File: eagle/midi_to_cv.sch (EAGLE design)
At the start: 46 parts, among them IC2 4504N, IC3 4099N, U1 ATMEGA328P_PDIP

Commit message: a manual start
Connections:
- net N$13: now also U1.PC2(ADC2); no longer U1.PC0(ADC0)
- net N$25: now also U1.PC0(ADC0); no longer U1.PC2(ADC2)
- net N$37: now also IC3A.!E; no longer IC3A.D
- net N$38: now also IC3A.D; no longer IC3A.!E
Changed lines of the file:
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@@
 <pinref part="IC2" gate="A" pin="DO"/>
 <wire x1="86.36" y1="66.04" x2="91.44" y2="66.04" width="0.1524" layer="91"/>
-<wire x1="91.44" y1="66.04" x2="91.44" y2="30.48" width="0.1524" layer="91"/>
-<pinref part="IC3" gate="A" pin="D"/>
-<wire x1="91.44" y1="30.48" x2="99.06" y2="30.48" width="0.1524" layer="91"/>
+<wire x1="91.44" y1="66.04" x2="91.44" y2="33.02" width="0.1524" layer="91"/>
+<pinref part="IC3" gate="A" pin="!E"/>
+<wire x1="99.06" y1="33.02" x2="91.44" y2="33.02" width="0.1524" layer="91"/>
 </segment>
 </net>
@@
 <pinref part="IC2" gate="A" pin="EO"/>
 <wire x1="86.36" y1="63.5" x2="88.9" y2="63.5" width="0.1524" layer="91"/>
-<wire x1="88.9" y1="63.5" x2="88.9" y2="33.02" width="0.1524" layer="91"/>
-<pinref part="IC3" gate="A" pin="!E"/>
-<wire x1="99.06" y1="33.02" x2="88.9" y2="33.02" width="0.1524" layer="91"/>
+<wire x1="88.9" y1="63.5" x2="88.9" y2="30.48" width="0.1524" layer="91"/>
+<pinref part="IC3" gate="A" pin="D"/>
+<wire x1="88.9" y1="30.48" x2="99.06" y2="30.48" width="0.1524" layer="91"/>
 </segment>
 </net>
@@
 </segment>
 </net>
-<net name="N$13" class="0">
-<segment>
-<pinref part="U1" gate="G$1" pin="PC0(ADC0)"/>
-<pinref part="IC2" gate="A" pin="CI"/>
-<wire x1="43.18" y1="73.66" x2="60.96" y2="68.58" width="0.1524" layer="91"/>
-</segment>
-</net>
 <net name="N$23" class="0">
 <segment>
@@
 <pinref part="U1" gate="G$1" pin="PC1(ADC1)"/>
 <wire x1="60.96" y1="71.12" x2="43.18" y2="71.12" width="0.1524" layer="91"/>
-</segment>
-</net>
-<net name="N$25" class="0">
-<segment>
-<pinref part="U1" gate="G$1" pin="PC2(ADC2)"/>
-<pinref part="IC2" gate="A" pin="AI"/>
-<wire x1="43.18" y1="68.58" x2="60.96" y2="73.66" width="0.1524" layer="91"/>
 </segment>
 </net>
@@
 </segment>
 </net>
+<net name="N$13" class="0">
+<segment>
+<pinref part="U1" gate="G$1" pin="PC2(ADC2)"/>
+<pinref part="IC2" gate="A" pin="CI"/>
+<wire x1="43.18" y1="68.58" x2="60.96" y2="68.58" width="0.1524" layer="91"/>
+</segment>
+</net>
+<net name="N$25" class="0">
+<segment>
+<pinref part="IC2" gate="A" pin="AI"/>
+<pinref part="U1" gate="G$1" pin="PC0(ADC0)"/>
+<wire x1="60.96" y1="73.66" x2="43.18" y2="73.66" width="0.1524" layer="91"/>
+</segment>
+</net>

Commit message: routed
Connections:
- removed net N$42: JP3.3, R20.2
- new net N$34: JP3.5, R20.2
- net N$37: now also IC3A.D; no longer IC3A.!E
- net N$38: now also IC3A.!E; no longer IC3A.D
- net N$40: now also JP3.1; no longer JP3.7
- net N$41: now also JP3.3; no longer JP3.5
- net N$51: now also JP3.7; no longer JP3.1
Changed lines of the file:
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@@
 <pinref part="IC2" gate="A" pin="DO"/>
 <wire x1="86.36" y1="66.04" x2="91.44" y2="66.04" width="0.1524" layer="91"/>
-<wire x1="91.44" y1="66.04" x2="91.44" y2="33.02" width="0.1524" layer="91"/>
-<pinref part="IC3" gate="A" pin="!E"/>
-<wire x1="99.06" y1="33.02" x2="91.44" y2="33.02" width="0.1524" layer="91"/>
+<wire x1="91.44" y1="66.04" x2="91.44" y2="30.48" width="0.1524" layer="91"/>
+<pinref part="IC3" gate="A" pin="D"/>
+<wire x1="91.44" y1="30.48" x2="99.06" y2="30.48" width="0.1524" layer="91"/>
 </segment>
 </net>
@@
 <pinref part="IC2" gate="A" pin="EO"/>
 <wire x1="86.36" y1="63.5" x2="88.9" y2="63.5" width="0.1524" layer="91"/>
-<wire x1="88.9" y1="63.5" x2="88.9" y2="30.48" width="0.1524" layer="91"/>
-<pinref part="IC3" gate="A" pin="D"/>
-<wire x1="88.9" y1="30.48" x2="99.06" y2="30.48" width="0.1524" layer="91"/>
+<wire x1="88.9" y1="63.5" x2="88.9" y2="33.02" width="0.1524" layer="91"/>
+<pinref part="IC3" gate="A" pin="!E"/>
+<wire x1="99.06" y1="33.02" x2="88.9" y2="33.02" width="0.1524" layer="91"/>
 </segment>
 </net>
@@
 <wire x1="132.08" y1="-10.16" x2="137.16" y2="-10.16" width="0.1524" layer="91"/>
 <wire x1="137.16" y1="-10.16" x2="137.16" y2="-17.78" width="0.1524" layer="91"/>
-<wire x1="137.16" y1="-17.78" x2="203.2" y2="-17.78" width="0.1524" layer="91"/>
-<wire x1="203.2" y1="-17.78" x2="203.2" y2="12.7" width="0.1524" layer="91"/>
-<pinref part="JP3" gate="A" pin="7"/>
-<wire x1="203.2" y1="12.7" x2="185.42" y2="12.7" width="0.1524" layer="91"/>
+<wire x1="137.16" y1="-17.78" x2="193.04" y2="-17.78" width="0.1524" layer="91"/>
+<wire x1="193.04" y1="-17.78" x2="193.04" y2="-2.54" width="0.1524" layer="91"/>
+<pinref part="JP3" gate="A" pin="1"/>
+<wire x1="185.42" y1="-2.54" x2="193.04" y2="-2.54" width="0.1524" layer="91"/>
 </segment>
 </net>
@@
 <wire x1="121.92" y1="-12.7" x2="134.62" y2="-12.7" width="0.1524" layer="91"/>
 <wire x1="134.62" y1="-12.7" x2="134.62" y2="-20.32" width="0.1524" layer="91"/>
-<wire x1="134.62" y1="-20.32" x2="200.66" y2="-20.32" width="0.1524" layer="91"/>
-<wire x1="200.66" y1="-20.32" x2="200.66" y2="7.62" width="0.1524" layer="91"/>
-<pinref part="JP3" gate="A" pin="5"/>
-<wire x1="200.66" y1="7.62" x2="185.42" y2="7.62" width="0.1524" layer="91"/>
-</segment>
-</net>
-<net name="N$42" class="0">
-<segment>
-<pinref part="R20" gate="G$1" pin="2"/>
-<wire x1="132.08" y1="-15.24" x2="132.08" y2="-22.86" width="0.1524" layer="91"/>
-<wire x1="132.08" y1="-22.86" x2="198.12" y2="-22.86" width="0.1524" layer="91"/>
-<wire x1="198.12" y1="-22.86" x2="198.12" y2="2.54" width="0.1524" layer="91"/>
+<wire x1="134.62" y1="-20.32" x2="195.58" y2="-20.32" width="0.1524" layer="91"/>
+<wire x1="195.58" y1="-20.32" x2="195.58" y2="2.54" width="0.1524" layer="91"/>
 <pinref part="JP3" gate="A" pin="3"/>
-<wire x1="198.12" y1="2.54" x2="185.42" y2="2.54" width="0.1524" layer="91"/>
+<wire x1="185.42" y1="2.54" x2="195.58" y2="2.54" width="0.1524" layer="91"/>
 </segment>
 </net>
@@
 <wire x1="121.92" y1="-17.78" x2="129.54" y2="-17.78" width="0.1524" layer="91"/>
 <wire x1="129.54" y1="-17.78" x2="129.54" y2="-25.4" width="0.1524" layer="91"/>
-<wire x1="129.54" y1="-25.4" x2="195.58" y2="-25.4" width="0.1524" layer="91"/>
-<wire x1="195.58" y1="-25.4" x2="195.58" y2="-2.54" width="0.1524" layer="91"/>
-<pinref part="JP3" gate="A" pin="1"/>
-<wire x1="195.58" y1="-2.54" x2="185.42" y2="-2.54" width="0.1524" layer="91"/>
+<wire x1="129.54" y1="-25.4" x2="200.66" y2="-25.4" width="0.1524" layer="91"/>
+<wire x1="200.66" y1="-25.4" x2="200.66" y2="12.7" width="0.1524" layer="91"/>
+<pinref part="JP3" gate="A" pin="7"/>
+<wire x1="200.66" y1="12.7" x2="185.42" y2="12.7" width="0.1524" layer="91"/>
 </segment>
 </net>
@@
 </segment>
 </net>
+<net name="N$34" class="0">
+<segment>
+<pinref part="JP3" gate="A" pin="5"/>
+<wire x1="198.12" y1="7.62" x2="185.42" y2="7.62" width="0.1524" layer="91"/>
+<pinref part="R20" gate="G$1" pin="2"/>
+<wire x1="132.08" y1="-15.24" x2="132.08" y2="-22.86" width="0.1524" layer="91"/>
+<wire x1="132.08" y1="-22.86" x2="198.12" y2="-22.86" width="0.1524" layer="91"/>
+<wire x1="198.12" y1="7.62" x2="198.12" y2="-22.86" width="0.1524" layer="91"/>
+</segment>
+</net>

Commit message: cutout
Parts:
- removed PAD11, PAD14: gate LED, wirepad:2,54/0,9
- added LED: 22-23-2021, con-molex:22-23-2021
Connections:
- removed net N$26: C4.-, C5.-, C6.2, C7.2, PWR1.GND
- net GND: now also C4.-, C5.-, C6.2, C7.2, LED-1.S, PWR1.GND; no longer PAD14.P
- net N$11: now also LED-2.S; no longer PAD11.P

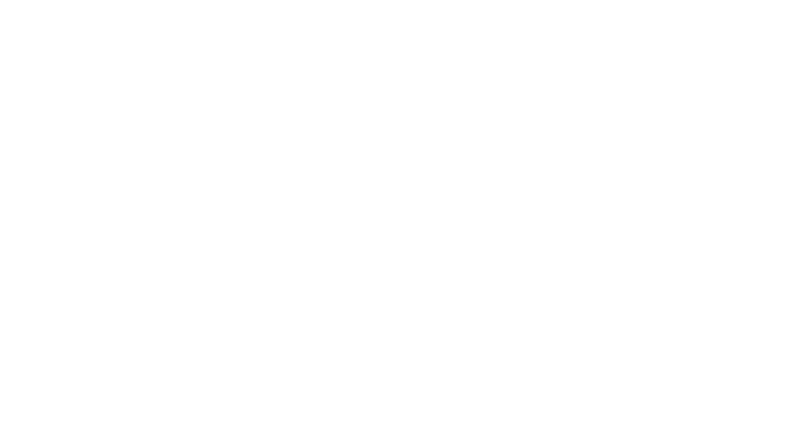
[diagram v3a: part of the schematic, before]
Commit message: created the device for ad8804 12ch dac
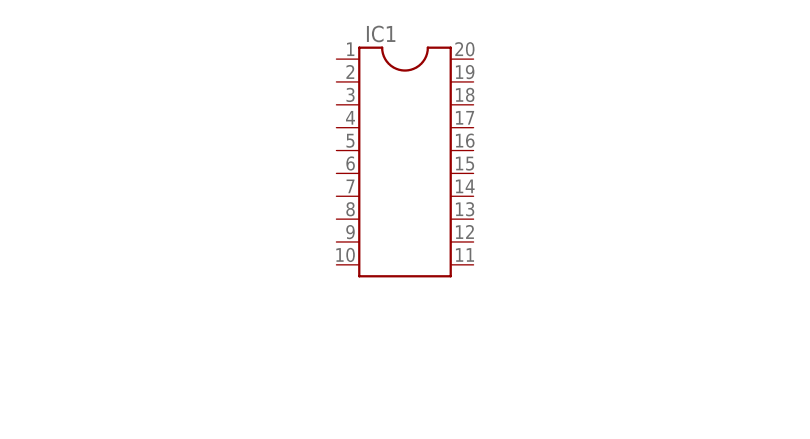
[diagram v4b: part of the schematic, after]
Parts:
- added IC1: (no value), ic-package:DIL20
- added U$1: AD8804, ic-package:AD8804
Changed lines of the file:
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@@
 <?xml version="1.0" encoding="utf-8"?>
 <!DOCTYPE eagle SYSTEM "eagle.dtd">
-<eagle version="7.2.0">
+<eagle version="7.1.0">
 <drawing>
 <settings>
@@
 <grid distance="0.1" unitdist="inch" unit="inch" style="lines" multiple="1" display="no" altdistance="0.01" altunitdist="inch" altunit="inch"/>
 <layers>
-<layer number="1" name="Top" color="4" fill="1" visible="no" active="no"/>
-<layer number="16" name="Bottom" color="1" fill="1" visible="no" active="no"/>
-<layer number="17" name="Pads" color="2" fill="1" visible="no" active="no"/>
-<layer number="18" name="Vias" color="2" fill="1" visible="no" active="no"/>
-<layer number="19" name="Unrouted" color="6" fill="1" visible="no" active="no"/>
-<layer number="20" name="Dimension" color="15" fill="1" visible="no" active="no"/>
-<layer number="21" name="tPlace" color="7" fill="1" visible="no" active="no"/>
-<layer number="22" name="bPlace" color="7" fill="1" visible="no" active="no"/>
-<layer number="23" name="tOrigins" color="15" fill="1" visible="no" active="no"/>
-<layer number="24" name="bOrigins" color="15" fill="1" visible="no" active="no"/>
-<layer number="25" name="tNames" color="7" fill="1" visible="no" active="no"/>
-<layer number="26" name="bNames" color="7" fill="1" visible="no" active="no"/>
-<layer number="27" name="tValues" color="7" fill="1" visible="no" active="no"/>
-<layer number="28" name="bValues" color="7" fill="1" visible="no" active="no"/>
+<layer number="1" name="Top" color="4" fill="1" visible="yes" active="no"/>
+<layer number="16" name="Bottom" color="1" fill="1" visible="yes" active="no"/>
+<layer number="17" name="Pads" color="2" fill="1" visible="yes" active="no"/>
+<layer number="18" name="Vias" color="2" fill="1" visible="yes" active="no"/>
+<layer number="19" name="Unrouted" color="6" fill="1" visible="yes" active="no"/>
+<layer number="20" name="Dimension" color="15" fill="1" visible="yes" active="no"/>
+<layer number="21" name="tPlace" color="7" fill="1" visible="yes" active="no"/>
+<layer number="22" name="bPlace" color="7" fill="1" visible="yes" active="no"/>
+<layer number="23" name="tOrigins" color="15" fill="1" visible="yes" active="no"/>
+<layer number="24" name="bOrigins" color="15" fill="1" visible="yes" active="no"/>
+<layer number="25" name="tNames" color="7" fill="1" visible="yes" active="no"/>
+<layer number="26" name="bNames" color="7" fill="1" visible="yes" active="no"/>
+<layer number="27" name="tValues" color="7" fill="1" visible="yes" active="no"/>
+<layer number="28" name="bValues" color="7" fill="1" visible="yes" active="no"/>
 <layer number="29" name="tStop" color="7" fill="3" visible="no" active="no"/>
 <layer number="30" name="bStop" color="7" fill="6" visible="no" active="no"/>
@@
 <layer number="35" name="tGlue" color="7" fill="4" visible="no" active="no"/>
 <layer number="36" name="bGlue" color="7" fill="5" visible="no" active="no"/>
-<layer number="37" name="tTest" color="7" fill="1" visible="no" active="no"/>
-<layer number="38" name="bTest" color="7" fill="1" visible="no" active="no"/>
+<layer number="37" name="tTest" color="7" fill="1" visible="yes" active="no"/>
+<layer number="38" name="bTest" color="7" fill="1" visible="yes" active="no"/>
 <layer number="39" name="tKeepout" color="4" fill="11" visible="no" active="no"/>
 <layer number="40" name="bKeepout" color="1" fill="11" visible="no" active="no"/>
@@
 <layer number="44" name="Drills" color="7" fill="1" visible="no" active="no"/>
 <layer number="45" name="Holes" color="7" fill="1" visible="no" active="no"/>
-<layer number="46" name="Milling" color="3" fill="1" visible="no" active="no"/>
-<layer number="47" name="Measures" color="7" fill="1" visible="no" active="no"/>
-<layer number="48" name="Document" color="7" fill="1" visible="no" active="no"/>
-<layer number="49" name="Reference" color="7" fill="1" visible="no" active="no"/>
-<layer number="50" name="dxf" color="7" fill="1" visible="no" active="no"/>
-<layer number="51" name="tDocu" color="7" fill="1" visible="no" active="no"/>
-<layer number="52" name="bDocu" color="7" fill="1" visible="no" active="no"/>
-<layer number="53" name="tGND_GNDA" color="7" fill="9" visible="no" active="no"/>
-<layer number="54" name="bGND_GNDA" color="1" fill="9" visible="no" active="no"/>
-<layer number="56" name="wert" color="7" fill="1" visible="no" active="no"/>
-<layer number="57" name="tCAD" color="7" fill="1" visible="no" active="no"/>
-<layer number="59" name="tCarbon" color="7" fill="1" visible="no" active="no"/>
-<layer number="60" name="bCarbon" color="7" fill="1" visible="no" active="no"/>
+<layer number="46" name="Milling" color="3" fill="1" visible="yes" active="no"/>
+<layer number="47" name="Measures" color="7" fill="1" visible="yes" active="no"/>
+<layer number="48" name="Document" color="7" fill="1" visible="yes" active="no"/>
+<layer number="49" name="Reference" color="7" fill="1" visible="yes" active="no"/>
+<layer number="50" name="dxf" color="7" fill="1" visible="yes" active="no"/>
+<layer number="51" name="tDocu" color="7" fill="1" visible="yes" active="no"/>
+<layer number="52" name="bDocu" color="7" fill="1" visible="yes" active="no"/>
+<layer number="53" name="tGND_GNDA" color="7" fill="9" visible="yes" active="no"/>
+<layer number="54" name="bGND_GNDA" color="1" fill="9" visible="yes" active="no"/>
+<layer number="56" name="wert" color="7" fill="1" visible="yes" active="no"/>
+<layer number="57" name="tCAD" color="7" fill="1" visible="yes" active="no"/>
+<layer number="59" name="tCarbon" color="7" fill="1" visible="yes" active="no"/>
+<layer number="60" name="bCarbon" color="7" fill="1" visible="yes" active="no"/>
 <layer number="90" name="Modules" color="5" fill="1" visible="yes" active="yes"/>
 <layer number="91" name="Nets" color="2" fill="1" visible="yes" active="yes"/>
@@
 <part name="GND7" library="supply1" deviceset="GND" device=""/>
 <part name="GND8" library="supply1" deviceset="GND" device=""/>
+<part name="IC1" library="ic-package" deviceset="DIL20" device=""/>
+<part name="U$1" library="ic-package" deviceset="AD8804" device=""/>
 </parts>
 <sheets>
@@
 <instance part="GND7" gate="1" x="50.8" y="96.52"/>
 <instance part="GND8" gate="1" x="60.96" y="96.52"/>
+<instance part="IC1" gate="G$1" x="160.02" y="114.3"/>
 </instances>
 <busses>

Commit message: midi thru
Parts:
- removed IC2: 4504N, 45xx:4504N
- removed IC3: 4099N, 40xx:4099N
- removed JP2, JP3: (no value), pinhead:PINHD-1X8
- removed R10, R11, R12, R13, R14, R16, R17, R18, R19, R20, R21, R3, R7, R8, R9: 1k, rcl:R-US_0207/10
- removed U$11: TLV5628C/I, Texas Instruments_By_element14_Batch_1:TLV5628C/I
- added IC4, IC5: TL074P, linear:TL074P
- added MIDI_OUT_THRU1: 22-23-2031, con-molex:22-23-2031
- IC1: value (none) -> TL074P; device ic-package:DIL20 -> linear:TL074P
- R2: value 1k -> 220
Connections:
- removed net N$13: IC2A.CI, U1.PC2(ADC2)
- removed net N$14: U$11.CLK, U1.PD7(AIN1)
- removed net N$15: U$11.~LOAD, U1.PB2(SS/OC1B)
- removed net N$16: JP3.4, R11.2
- removed net N$21: JP3.2, R12.2
- removed net N$22: JP2.7, R13.2
- removed net N$23: IC2A.BI, U1.PC1(ADC1)
- removed net N$24: JP2.5, R14.2
- removed net N$25: IC2A.AI, U1.PC0(ADC0)
- removed net N$27: U$11.DATA, U1.PB0(ICP)
- removed net N$28: JP2.3, R16.2
- removed net N$29: JP2.1, R17.2
- removed net N$30: IC2A.DI, U1.PC5(ADC5/SCL)
- removed net N$31: IC2A.FI, U1.PC3(ADC3)
- removed net N$32: IC2A.EI, U1.PC4(ADC4/SDA)
- removed net N$33: IC2A.CO, IC3A.A0
- removed net N$34: JP3.5, R20.2
- removed net N$35: IC2A.BO, IC3A.A1
- removed net N$36: IC2A.AO, IC3A.A2
- removed net N$37: IC2A.DO, IC3A.D
- removed net N$38: IC2A.EO, IC3A.!E
- removed net N$39: IC3A.Q0, R2.1
- removed net N$40: JP3.1, R18.2
- removed net N$41: JP3.3, R19.2
- removed net N$44: IC3A.Q1, R3.1
- removed net N$45: IC3A.Q2, R7.1
- removed net N$46: IC3A.Q3, R8.1
- removed net N$47: IC3A.Q4, R9.1
- removed net N$48: IC3A.Q5, R10.1
- removed net N$49: IC3A.Q6, R11.1
- removed net N$50: IC3A.Q7, R12.1
- removed net N$51: JP3.7, R21.2
- removed net N$52: R13.1, U$11.OUTA
- removed net N$53: R14.1, U$11.OUTB
- removed net N$54: R16.1, U$11.OUTC
- removed net N$55: R17.1, U$11.OUTD
- removed net N$56: R18.1, U$11.OUTE
- removed net N$57: R19.1, U$11.OUTF
- removed net N$58: R20.1, U$11.OUTG
- removed net N$59: R21.1, U$11.OUTH
- removed net N$61: IC2A.FO, IC3A.CLR
- net +12V: no longer IC2P.VDD, IC3P.VDD
- net +5V: now also R2.1, U$1.VDD, U$1.V_REF_H; no longer IC2A.MODE, IC2P.VCC, U$11.REF1, U$11.REF2, U$11.VDD
- net GND: now also MIDI_OUT_THRU1-3.S, U$1.GND, U$1.V_REF_L; no longer IC2P.GND, IC3P.VSS, U$11.GND, U$11.~LDAC
- net N$12: now also MIDI_OUT_THRU1-2.S, U1.PD1(TXD); no longer JP3.6, R10.2
- net N$3: now also U$1.~SHDN, U1.PC0(ADC0); no longer JP2.8, R2.2
- net N$6: now also U$1.~CS, U1.PC1(ADC1); no longer JP2.6, R3.2
- net N$7: now also U$1.CLK, U1.PC2(ADC2); no longer JP2.4, R7.2
- net N$8: now also U$1.SDI, U1.PC3(ADC3); no longer JP2.2, R8.2
- net N$9: now also MIDI_OUT_THRU1-1.S, R2.2; no longer JP3.8, R9.2
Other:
- moved on the sheet: R2
